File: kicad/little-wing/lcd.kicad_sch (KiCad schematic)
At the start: 9 parts, among them J5 Conn_01x10

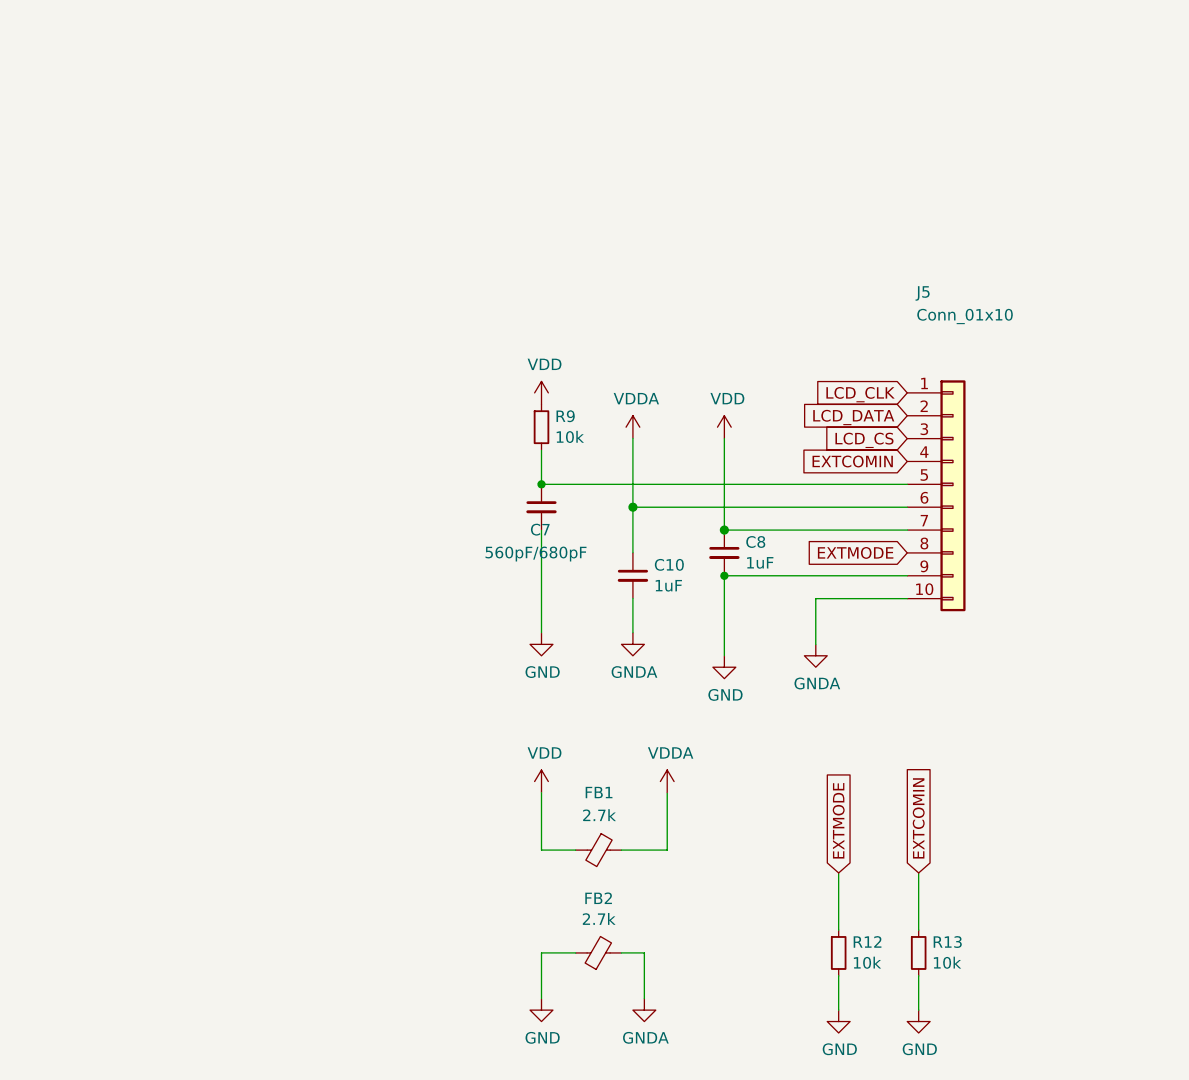
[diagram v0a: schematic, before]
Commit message: Cleaning up the schematics a bit more
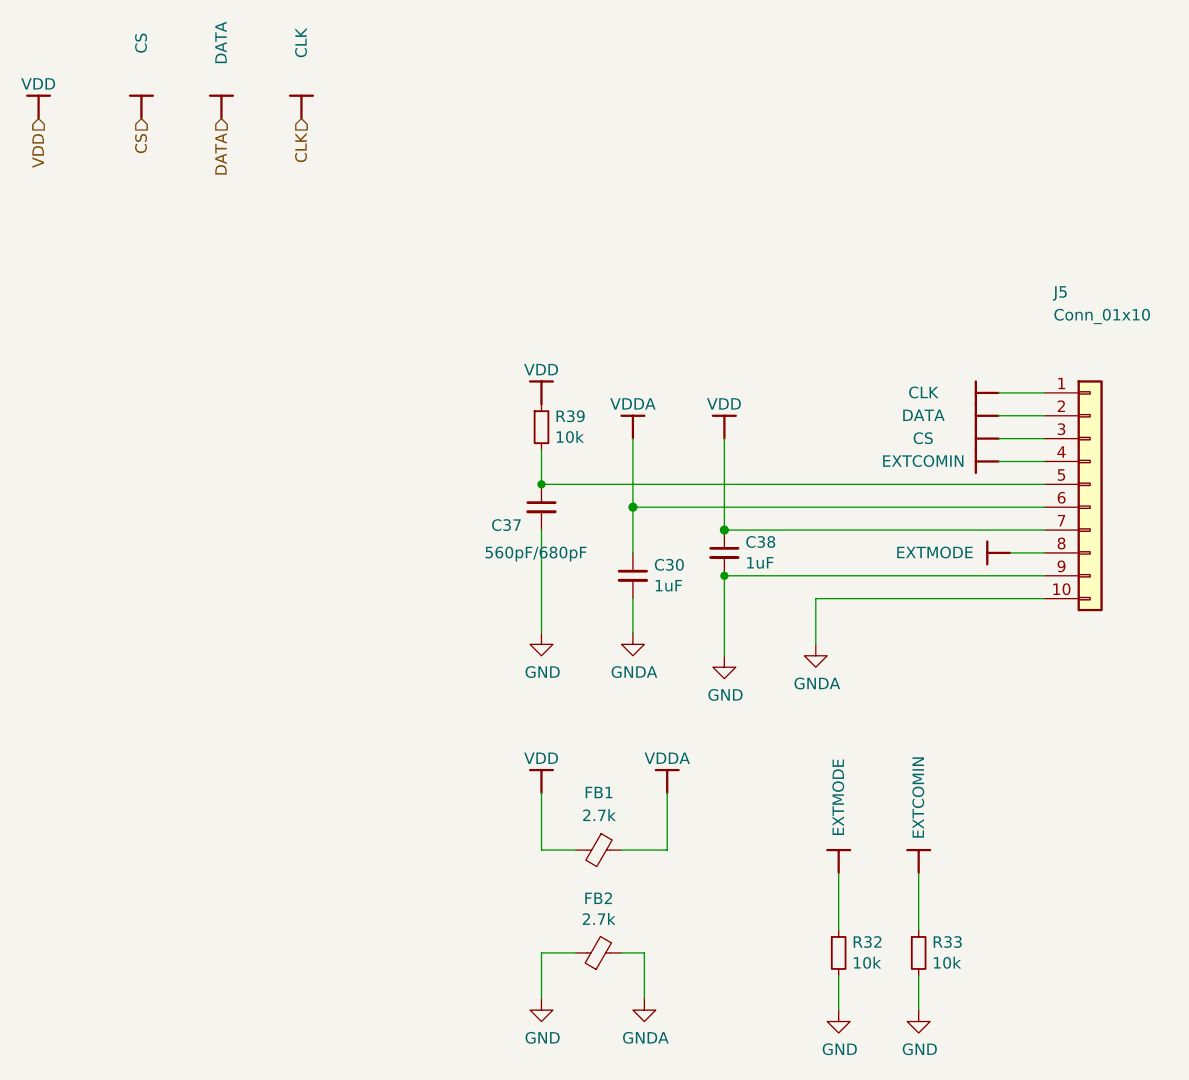
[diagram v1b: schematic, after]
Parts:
- renumbered C10 to C30, C7 to C37, C8 to C38, R12 to R32, R13 to R33, R9 to R39
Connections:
- net LCD_CLK renamed CLK
- net LCD_CS renamed CS
- net LCD_DATA renamed DATA
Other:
- moved on the sheet: J5

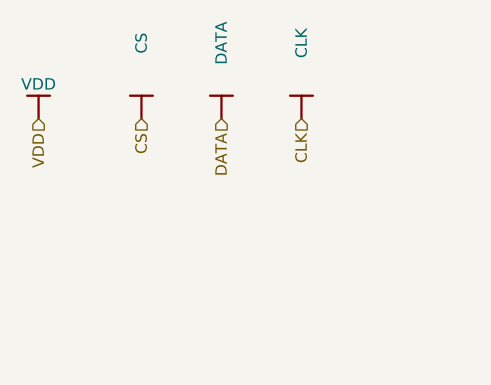
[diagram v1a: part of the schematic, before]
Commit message: Updating schematics/pcb to match the labels
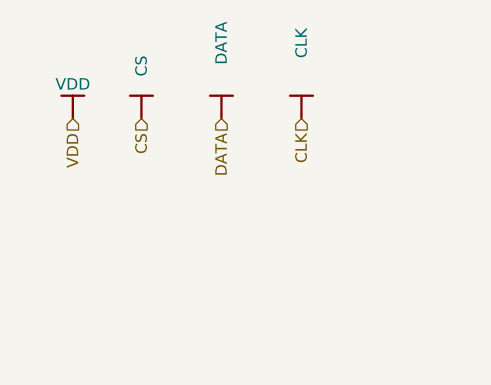
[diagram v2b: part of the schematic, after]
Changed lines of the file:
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@@
 	(hierarchical_label "VDD"
 		(shape input)
-		(at 49.53 33.02 270)
+		(at 53.34 33.02 270)
 		(effects
 			(font
@@
 	(symbol
 		(lib_id "npm1100_caax_config1-altium-import:VBUS_BAR")
-		(at 49.53 33.02 180)
+		(at 53.34 33.02 180)
 		(unit 1)
 		(exclude_from_sim no)
@@
 		(dnp no)
 		(property "Reference" "#PWR069"
-			(at 49.53 33.02 0)
+			(at 53.34 33.02 0)
 			(effects
 				(font
@@
 		)
 		(property "Value" "VDD"
-			(at 49.53 29.21 0)
-			(effects
-				(font
-					(size 1.27 1.27)
-				)
-			)
-		)
-		(property "Footprint" ""
-			(at 49.53 33.02 0)
-			(effects
-				(font
-					(size 1.27 1.27)
-				)
-			)
-		)
-		(property "Datasheet" ""
-			(at 49.53 33.02 0)
-			(effects
-				(font
-					(size 1.27 1.27)
-				)
-			)
-		)
-		(property "Description" ""
-			(at 49.53 33.02 0)
+			(at 53.34 29.21 0)
+			(effects
+				(font
+					(size 1.27 1.27)
+				)
+			)
+		)
+		(property "Footprint" ""
+			(at 53.34 33.02 0)
+			(effects
+				(font
+					(size 1.27 1.27)
+				)
+			)
+		)
+		(property "Datasheet" ""
+			(at 53.34 33.02 0)
+			(effects
+				(font
+					(size 1.27 1.27)
+				)
+			)
+		)
+		(property "Description" ""
+			(at 53.34 33.02 0)
 			(effects
 				(font
@@
 		)
 		(property "Value" "CS"
-			(at 60.96 24.638 90)
-			(effects
-				(font
+			(at 60.96 27.178 90)
+			(effects
+				(font

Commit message: Reseting all the extra components sizes
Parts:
- C30, C37, C38: footprint Capacitor_SMD:C_0603_1608Metric_Pad1.08x0.95mm_HandSolder -> Capacitor_SMD:C_0201_0603Metric
- FB1, FB2: footprint Resistor_SMD:R_0805_2012Metric_Pad1.20x1.40mm_HandSolder -> Resistor_SMD:R_0402_1005Metric
- R32, R33, R39: footprint Resistor_SMD:R_0603_1608Metric_Pad0.98x0.95mm_HandSolder -> Resistor_SMD:R_0201_0603Metric
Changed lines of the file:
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@@
 			)
 		)
-		(property "Footprint" "Resistor_SMD:R_0805_2012Metric_Pad1.20x1.40mm_HandSolder"
+		(property "Footprint" "Resistor_SMD:R_0402_1005Metric"
 			(at 111.76 127.508 90)
 			(effects
@@
 			)
 		)
-		(property "Footprint" "Resistor_SMD:R_0805_2012Metric_Pad1.20x1.40mm_HandSolder"
+		(property "Footprint" "Resistor_SMD:R_0402_1005Metric"
 			(at 111.76 112.522 90)
 			(effects
@@
 			)
 		)
-		(property "Footprint" "Capacitor_SMD:C_0603_1608Metric_Pad1.08x0.95mm_HandSolder"
+		(property "Footprint" "Capacitor_SMD:C_0201_0603Metric"
 			(at 115.57 83.82 0)
 			(effects
@@
 			)
 		)
-		(property "Footprint" "Resistor_SMD:R_0603_1608Metric_Pad0.98x0.95mm_HandSolder"
+		(property "Footprint" "Resistor_SMD:R_0201_0603Metric"
 			(at 105.41 67.31 0)
 			(effects
@@
 			)
 		)
-		(property "Footprint" "Resistor_SMD:R_0603_1608Metric_Pad0.98x0.95mm_HandSolder"
+		(property "Footprint" "Resistor_SMD:R_0201_0603Metric"
 			(at 138.43 125.73 0)
 			(effects
@@
 			)
 		)
-		(property "Footprint" "Capacitor_SMD:C_0603_1608Metric_Pad1.08x0.95mm_HandSolder"
+		(property "Footprint" "Capacitor_SMD:C_0201_0603Metric"
 			(at 105.41 76.2 0)
 			(effects
@@
 			)
 		)
-		(property "Footprint" "Capacitor_SMD:C_0603_1608Metric_Pad1.08x0.95mm_HandSolder"
+		(property "Footprint" "Capacitor_SMD:C_0201_0603Metric"
 			(at 125.73 81.28 0)
 			(effects
@@
 			)
 		)
-		(property "Footprint" "Resistor_SMD:R_0603_1608Metric_Pad0.98x0.95mm_HandSolder"
+		(property "Footprint" "Resistor_SMD:R_0201_0603Metric"
 			(at 147.32 125.73 0)
 			(effects

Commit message: Backporting footprints from the PCB back to schematic
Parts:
- J5: footprint Connector_FFC-FPC:Hirose_FH12-10S-0.5SH_1x10-1MP_P0.50mm_Horizontal -> Hirose FH34SRJ-10S-0.5SH:CONN10x1_FH34SRJ-10S-0.5SH50_HIR
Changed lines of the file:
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@@
 			)
 		)
-		(property "Footprint" "Connector_FFC-FPC:Hirose_FH12-10S-0.5SH_1x10-1MP_P0.50mm_Horizontal"
+		(property "Footprint" "Hirose FH34SRJ-10S-0.5SH:CONN10x1_FH34SRJ-10S-0.5SH50_HIR"
 			(at 166.37 73.66 0)
 			(effects
